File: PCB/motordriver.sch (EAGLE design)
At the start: 6 parts

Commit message: work in PCB
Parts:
- added 100K: 55k, myLibrary:RESISTOR0805_SMD
- added 100K1: 150k, myLibrary:RESISTOR0805_SMD
- added AC1~, AC2~, IN1, IN2, OUT, OUT1: SMDPAD, myLibrary:SMDPAD
- added B1: RECTIFIER-GBU4, rectifier:RECTIFIER-GBU4
- added BC47HFE=10000: MMBTA14LT1, transistor-npn:MMBTA14LT1
- added BC846, BC846$: (no value), semicon-smd-ipc:NPN-TRANSISTOR_SOT23
- added C1: 10000uF/25V, rcl:CPOL-EUE7.5-18
- added C2: 0.1uF, rcl:C-EUC1206
- added C3: 0.330uF, rcl:C-EUC1206
- added C4, C6: 47nF, rcl:C-EUC1206K
- added C5: 1uF, rcl:C-EUC1206K
- added C7: 100nF, rcl:C-EUC1206
- added FUSE: 100mA(hold), myLibrary:RESISTOR0805_SMD
- added GREEN_LED, RED_LED: (no value), led:LEDCHIPLED_0805
- added IC1: 7818TV, linear:7818TV
- added JMP1, JMP2, JMP3: 0R-JUMPA, jump-0r-smd:0R-JUMPA
- added R5, R6: 420 Ohm, myLibrary:RESISTOR0805_SMD
- added R7: 68k 1%, resistor:R-EU_R0805
- added R8: 10k, resistor:R-EU_R0805
- added R9: 12k, myLibrary:RESISTOR0805_SMD
- added U$3: POWER_LED, myLibrary:POWER_LED
- R1: value (none) -> 320
- R2: value (none) -> 10k
- R3: value (none) -> 132
- R4: value (none) -> 7 2W; device eagle-ltspice:R -> resistor:R-EU_R1210
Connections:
- new net +12V: B1.+, C1.+, C3.1, C6.1, IC1.VI, U$2.VM_A, U$2.VM_B
- new net +5V: C2.1, FUSE.P$1, IC1.VO, R1.P$1, R3.P$1, R4.1
- new net 120MA: BC47HFE=10000.C, U$3.CATHODE
- new net 22MA: BC846$.C, RED_LED.C
- new net 3.3V: R2.P$2, R8.1, U$1.3.3V
- new net 5MA: BC846.C, GREEN_LED.C
- new net BUTTON: C7.1, IN1.P$1, R2.P$1
- new net DVDD: C5.2, JMP1-0R.1, JMP2-0R.1, JMP3-0R.1, U$2.DVDD
- new net GND: B1.-, BC47HFE=10000.E, BC846$.E, BC846.E, C1.-, C2.2, C3.2, C5.1, C7.2, IC1.GND, IN2.P$1, JMP1-0R.3, JMP2-0R.3, JMP3-0R.3, R5.P$1, R6.P$1, R7.1, U$2.GND, U$2.SRC-A, U$2.SRC-B
- new net N$10: R7.2, U$2.SR
- new net N$11: C6.2, U$2.VCP
- new net N$12: OUT1.P$1, U$2.OUT2, U$2.OUT2B
- new net N$13: OUT.P$1, U$2.OUT1, U$2.OUT1B
- new net N$14: R3.P$2, RED_LED.A
- new net N$15: GREEN_LED.A, R1.P$2
- new net N$18: BC846$.B, R9.P$2
- new net N$19: R9.P$1
- new net N$2: AC2~.P$1, B1.AC2
- new net N$20: 100K.P$2, BC846.B
- new net N$21: 100K.P$1
- new net N$23: R4.2, U$3.ANODE
- new net N$24: 100K1.P$2, BC47HFE=10000.B
- new net N$25: 100K1.P$1
- new net N$26: FUSE.P$2, U$1.PB9
- new net N$3: C4.1, U$2.CPH
- new net N$4: C4.2, U$2.CPL
- new net N$5: JMP2-0R.2, U$2.NOL
- new net N$6: R6.P$2, U$2.IPROPI2
- new net N$7: R5.P$2, U$2.IPROPI1
- new net N$8: JMP1-0R.2, U$2.NITRIP
- new net N$9: JMP3-0R.2, U$2.MODE
- new net TOARM: R8.2, U$2.NFAULT
- net N$1: now also AC1~.P$1, B1.AC1; no longer U$1.GND1
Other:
- moved on the sheet: R4, U$2

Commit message: work in board
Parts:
- added AC1~1, AC2~1, IN3, IN4, OUT2, OUT3: SMDPAD, myLibrary:SMDPAD
- added C8, C9: 100nF, rcl:C-EUC0805
- C6: value 47nF -> 1uF
- renumbered 100K to R10
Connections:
- removed net BUTTON: C7.1, IN1.P$1, R2.P$1
- removed net N$19: R9.P$1
- removed net N$21: R10.P$1
- removed net N$25: 100K1.P$1
- removed net N$6: R6.P$2, U$2.IPROPI2
- removed net N$7: R5.P$2, U$2.IPROPI1
- new net PA0: R6.P$2, U$1.PA0, U$2.IPROPI2
- new net PA1: R5.P$2, U$1.PA1, U$2.IPROPI1
- new net PA15: C7.1, IN1.P$1, IN3.P$1, R2.P$1, U$1.PA15
- new net PB0: U$1.PB0
- new net PB11: U$1.PB11, U$2.NSLEEP
- new net PB12: R9.P$1, U$1.PB12
- new net PB13: R10.P$1, U$1.PB13
- new net PB14: 100K1.P$1, U$1.PB14
- new net PB3: U$1.PB3
- new net PB4: U$1.PB4, U$2.DISABLE
- new net PB8: U$1.PB8, U$2.PH/IN2
- new net PB9: U$1.PB9, U$2.EN/IN1
- net +12V: now also C8.2, C9.1
- net GND: now also C8.1, C9.2, IN4.P$1, U$1.GND, U$1.GND1, U$1.GND2
- net N$1: now also AC1~1.P$1
- net N$12: now also OUT3.P$1
- net N$13: now also OUT2.P$1
- net N$2: now also AC2~1.P$1
- net N$26: now also U$1.5V; no longer U$1.PB9
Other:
- moved on the sheet: FUSE

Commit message: more work in board
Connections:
- net 3.3V: now also U$1.3.3V1
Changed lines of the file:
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@@
 <label x="-8.78" y="189.04" size="1.778" layer="95"/>
+</segment>
+<segment>
+<pinref part="U$1" gate="G$1" pin="3.3V1"/>
+<wire x1="124.46" y1="91.44" x2="124.46" y2="88.9" width="0.1524" layer="91"/>
+<label x="127" y="86.36" size="1.778" layer="95"/>
 </segment>
 </net>

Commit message: more work in board
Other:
- moved on the sheet: U$2
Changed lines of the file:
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@@
 <grid distance="0.1" unitdist="inch" unit="inch" style="lines" multiple="1" display="no" altdistance="0.01" altunitdist="inch" altunit="inch"/>
 <layers>
-<layer number="1" name="Top" color="4" fill="1" visible="yes" active="no"/>
-<layer number="16" name="Bottom" color="1" fill="1" visible="yes" active="no"/>
-<layer number="17" name="Pads" color="2" fill="1" visible="yes" active="no"/>
-<layer number="18" name="Vias" color="2" fill="1" visible="yes" active="no"/>
-<layer number="19" name="Unrouted" color="6" fill="1" visible="yes" active="no"/>
-<layer number="20" name="Dimension" color="24" fill="1" visible="yes" active="no"/>
-<layer number="21" name="tPlace" color="7" fill="1" visible="yes" active="no"/>
-<layer number="22" name="bPlace" color="7" fill="1" visible="yes" active="no"/>
-<layer number="23" name="tOrigins" color="15" fill="1" visible="yes" active="no"/>
-<layer number="24" name="bOrigins" color="15" fill="1" visible="yes" active="no"/>
-<layer number="25" name="tNames" color="7" fill="1" visible="yes" active="no"/>
-<layer number="26" name="bNames" color="7" fill="1" visible="yes" active="no"/>
-<layer number="27" name="tValues" color="7" fill="1" visible="yes" active="no"/>
-<layer number="28" name="bValues" color="7" fill="1" visible="yes" active="no"/>
+<layer number="1" name="Top" color="4" fill="1" visible="no" active="no"/>
+<layer number="16" name="Bottom" color="1" fill="1" visible="no" active="no"/>
+<layer number="17" name="Pads" color="2" fill="1" visible="no" active="no"/>
+<layer number="18" name="Vias" color="2" fill="1" visible="no" active="no"/>
+<layer number="19" name="Unrouted" color="6" fill="1" visible="no" active="no"/>
+<layer number="20" name="Dimension" color="24" fill="1" visible="no" active="no"/>
+<layer number="21" name="tPlace" color="7" fill="1" visible="no" active="no"/>
+<layer number="22" name="bPlace" color="7" fill="1" visible="no" active="no"/>
+<layer number="23" name="tOrigins" color="15" fill="1" visible="no" active="no"/>
+<layer number="24" name="bOrigins" color="15" fill="1" visible="no" active="no"/>
+<layer number="25" name="tNames" color="7" fill="1" visible="no" active="no"/>
+<layer number="26" name="bNames" color="7" fill="1" visible="no" active="no"/>
+<layer number="27" name="tValues" color="7" fill="1" visible="no" active="no"/>
+<layer number="28" name="bValues" color="7" fill="1" visible="no" active="no"/>
 <layer number="29" name="tStop" color="7" fill="3" visible="no" active="no"/>
 <layer number="30" name="bStop" color="7" fill="6" visible="no" active="no"/>
@@
 <layer number="35" name="tGlue" color="7" fill="4" visible="no" active="no"/>
 <layer number="36" name="bGlue" color="7" fill="5" visible="no" active="no"/>
-<layer number="37" name="tTest" color="7" fill="1" visible="yes" active="no"/>
-<layer number="38" name="bTest" color="7" fill="1" visible="yes" active="no"/>
+<layer number="37" name="tTest" color="7" fill="1" visible="no" active="no"/>
+<layer number="38" name="bTest" color="7" fill="1" visible="no" active="no"/>
 <layer number="39" name="tKeepout" color="4" fill="11" visible="no" active="no"/>
 <layer number="40" name="bKeepout" color="1" fill="11" visible="no" active="no"/>
@@
 <layer number="44" name="Drills" color="7" fill="1" visible="no" active="no"/>
 <layer number="45" name="Holes" color="7" fill="1" visible="no" active="no"/>
-<layer number="46" name="Milling" color="3" fill="1" visible="yes" active="no"/>
-<layer number="47" name="Measures" color="7" fill="1" visible="yes" active="no"/>
-<layer number="48" name="Document" color="7" fill="1" visible="yes" active="no"/>
-<layer number="49" name="Reference" color="7" fill="1" visible="yes" active="no"/>
-<layer number="51" name="tDocu" color="7" fill="1" visible="yes" active="no"/>
-<layer number="52" name="bDocu" color="7" fill="1" visible="yes" active="no"/>
+<layer number="46" name="Milling" color="3" fill="1" visible="no" active="no"/>
+<layer number="47" name="Measures" color="7" fill="1" visible="no" active="no"/>
+<layer number="48" name="Document" color="7" fill="1" visible="no" active="no"/>
+<layer number="49" name="Reference" color="7" fill="1" visible="no" active="no"/>
+<layer number="51" name="tDocu" color="7" fill="1" visible="no" active="no"/>
+<layer number="52" name="bDocu" color="7" fill="1" visible="no" active="no"/>
 <layer number="88" name="SimResults" color="9" fill="1" visible="yes" active="yes"/>
 <layer number="89" name="SimProbes" color="9" fill="1" visible="yes" active="yes"/>

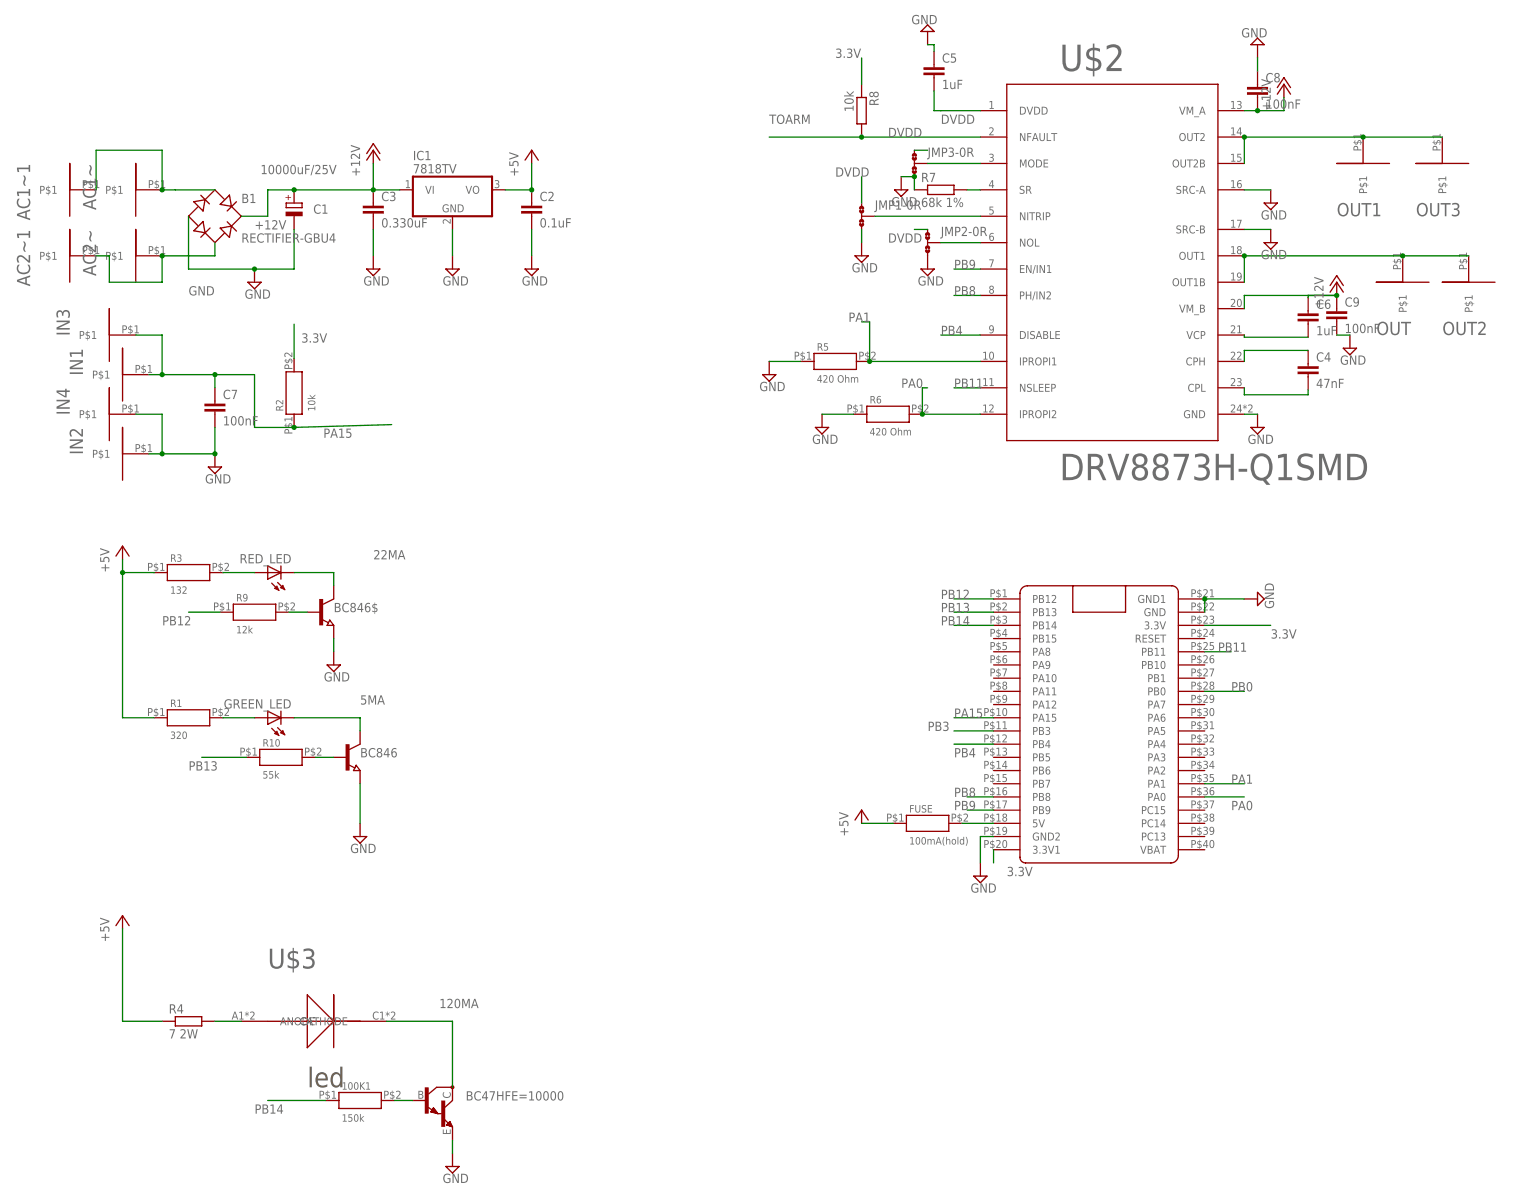
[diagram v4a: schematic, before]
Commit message: merge with eclipse, Matlab PCB.
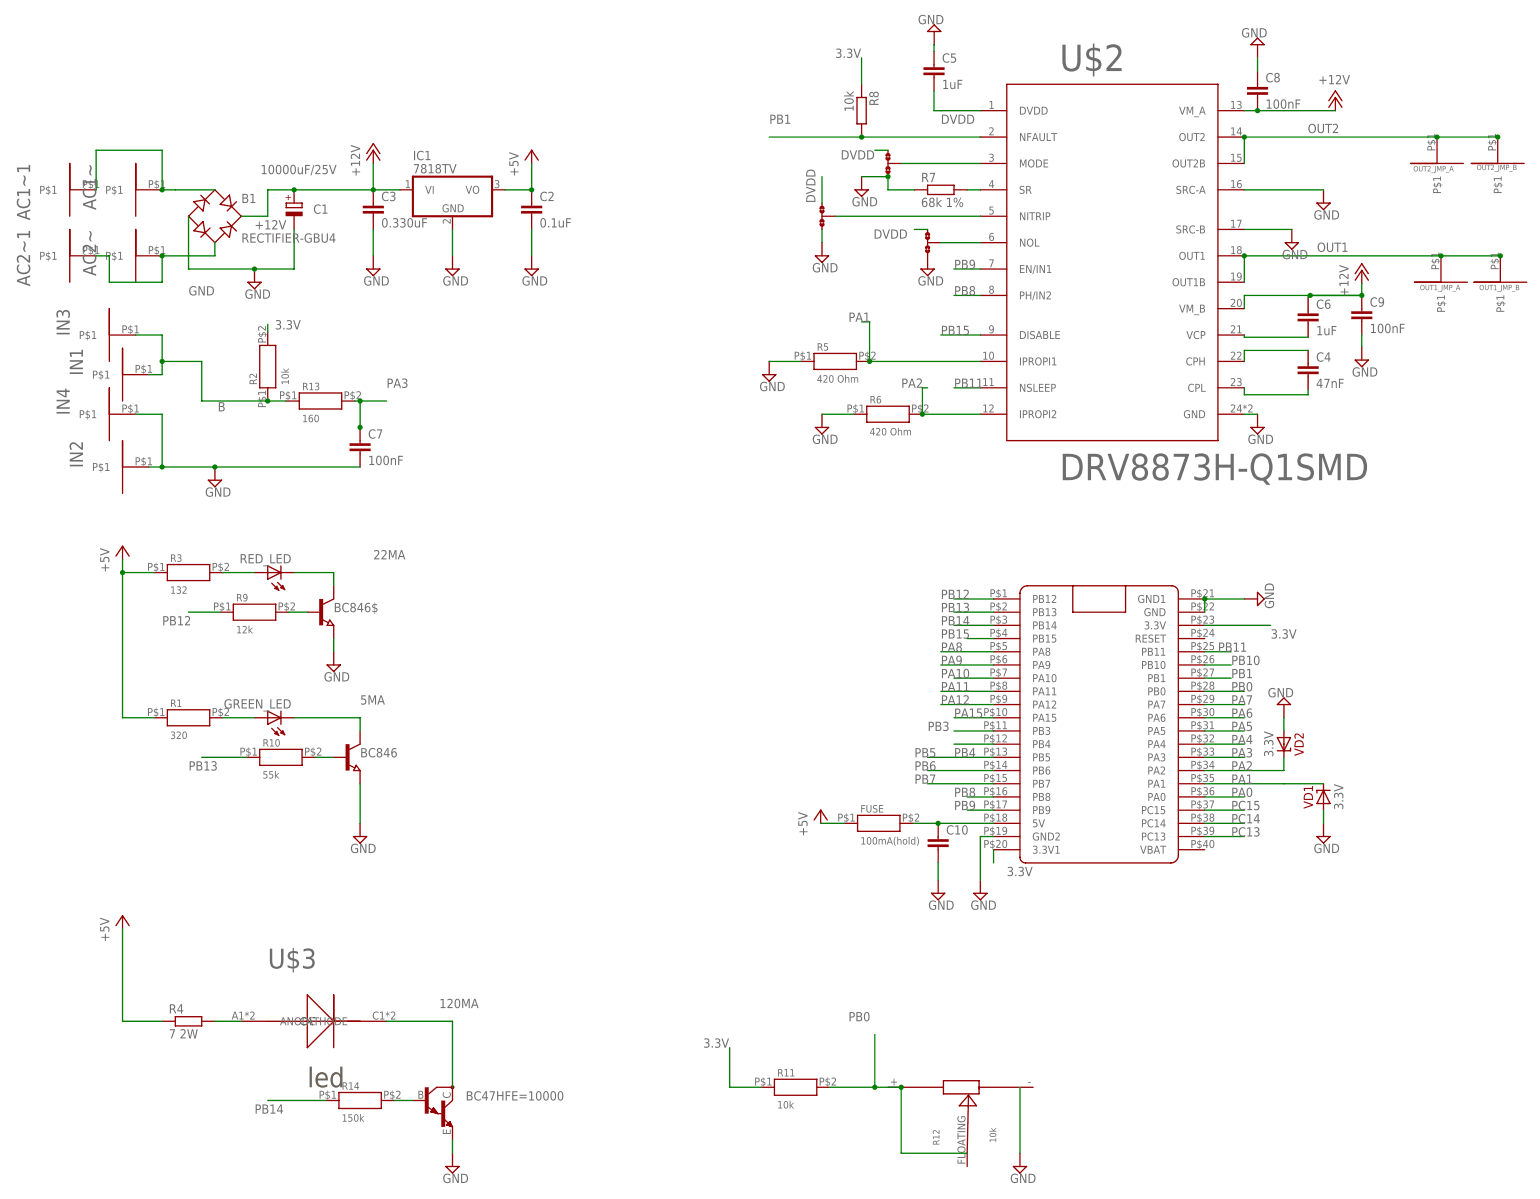
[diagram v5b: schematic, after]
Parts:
- removed OUT, OUT1, OUT2, OUT3: SMDPAD, myLibrary:SMDPAD
- added C10: (no value), rcl:C-EUC0805K
- added OUT1_JMP_A, OUT1_JMP_B, OUT2_JMP_A, OUT2_JMP_B: SMDPAD, myLibrary:SMDPAD
- added R11: 10k, myLibrary:RESISTOR0805_SMD
- added R12: 10k, myLibrary:POTENTIOMETER
- added R13: 160, myLibrary:RESISTOR0805_SMD
- added VD1, VD2: 3.3V, zener:5.6V(1N5232)
- renumbered 100K1 to R14
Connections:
- removed net N$12: OUT1.P$1, OUT3.P$1, U$2.OUT2, U$2.OUT2B
- removed net N$13: OUT.P$1, OUT2.P$1, U$2.OUT1, U$2.OUT1B
- removed net TOARM: R8.2, U$2.NFAULT
- new net B: IN1.P$1, IN3.P$1, R13.P$1, R2.P$1
- new net OUT1: OUT1_JMP_A.P$1, OUT1_JMP_B.P$1, U$2.OUT1, U$2.OUT1B
- new net OUT2: OUT2_JMP_A.P$1, OUT2_JMP_B.P$1, U$2.OUT2, U$2.OUT2B
- new net PA10: U$1.PA10
- new net PA11: U$1.PA11
- new net PA12: U$1.PA12
- new net PA2: R6.P$2, U$1.PA2, U$2.IPROPI2, VD2.C
- new net PA3: C7.1, R13.P$2, U$1.PA3
- new net PA4: U$1.PA4
- new net PA5: U$1.PA5
- new net PA6: U$1.PA6
- new net PA7: U$1.PA7
- new net PA8: U$1.PA8
- new net PA9: U$1.PA9
- new net PB1: R8.2, U$1.PB1, U$2.NFAULT
- new net PB10: U$1.PB10
- new net PB15: U$1.PB15, U$2.DISABLE
- new net PB5: U$1.PB5
- new net PB6: U$1.PB6
- new net PB7: U$1.PB7
- new net PC13: U$1.PC13
- new net PC14: U$1.PC14
- new net PC15: U$1.PC15
- net 3.3V: now also R11.P$1
- net GND: now also C10.2, R12.-, VD1.A, VD2.A
- net N$26: now also C10.1
- net PA0: no longer R6.P$2, U$2.IPROPI2
- net PA1: now also VD1.C
- net PA15: no longer C7.1, IN1.P$1, IN3.P$1, R2.P$1
- net PB0: now also R11.P$2, R12.+, R12.FLOATING
- net PB4: no longer U$2.DISABLE
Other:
- moved on the sheet: C7, C9, FUSE, IN2, R2

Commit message: some changes in resistor values.
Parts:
- C10: value (none) -> 100nF
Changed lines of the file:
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@@
 <part name="SUPPLY24" library="supply2" library_urn="urn:adsk.eagle:library:372" deviceset="GND" device=""/>
 <part name="R13" library="myLibrary" deviceset="RESISTOR" device="0805_SMD" value="160"/>
-<part name="C10" library="rcl" library_urn="urn:adsk.eagle:library:334" deviceset="C-EU" device="C0805K" package3d_urn="urn:adsk.eagle:package:23681/2"/>
+<part name="C10" library="rcl" library_urn="urn:adsk.eagle:library:334" deviceset="C-EU" device="C0805K" package3d_urn="urn:adsk.eagle:package:23681/2" value="100nF"/>
 <part name="SUPPLY25" library="supply2" library_urn="urn:adsk.eagle:library:372" deviceset="GND" device=""/>
 </parts>

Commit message: software is working. Send the sum of Iprop1 and Iprop2 to application software.
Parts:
- R5, R6: value 420 Ohm -> 402 Ohm
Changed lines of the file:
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@@
 <part name="C5" library="rcl" library_urn="urn:adsk.eagle:library:334" deviceset="C-EU" device="C1206K" package3d_urn="urn:adsk.eagle:package:23682/2" value="1uF"/>
 <part name="SUPPLY5" library="supply2" library_urn="urn:adsk.eagle:library:372" deviceset="GND" device=""/>
-<part name="R5" library="myLibrary" deviceset="RESISTOR" device="0805_SMD" value="420 Ohm"/>
-<part name="R6" library="myLibrary" deviceset="RESISTOR" device="0805_SMD" value="420 Ohm"/>
+<part name="R5" library="myLibrary" deviceset="RESISTOR" device="0805_SMD" value="402 Ohm"/>
+<part name="R6" library="myLibrary" deviceset="RESISTOR" device="0805_SMD" value="402 Ohm"/>
 <part name="JMP1" library="jump-0r-smd" library_urn="urn:adsk.eagle:library:251" deviceset="0R-JUMP" device="A" package3d_urn="urn:adsk.eagle:package:15385/1"/>
 <part name="SUPPLY6" library="supply2" library_urn="urn:adsk.eagle:library:372" deviceset="GND" device=""/>
